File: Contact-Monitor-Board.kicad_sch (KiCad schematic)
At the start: 82 parts, among them J1 JST VH 02, J10 JST VH 02, J11 JST VH 02, J12 JST VH 02, J13 JST VH 02, J14 JST VH 02, J15 JST VH 02, J16 JST VH 02, J17 header 4, J2 JST VH 02, J3 JST VH 02, J4 JST VH 02, J5 JST VH 02, J6 JST VH 02, J7 JST VH 02, J8 JST VH 02, J9 JST VH 02, Q1 2N7002, Q10 2N7002, Q11 2N7002, Q12 2N7002, Q13 2N7002, Q14 2N7002, Q15 2N7002, Q16 2N7002, Q2 2N7002, Q3 2N7002, Q4 2N7002, Q5 2N7002, Q6 2N7002, Q7 2N7002, Q8 2N7002, Q9 2N7002, SW1 KH-SS12D01-G3-5.0, U1 74HC4017D, U2 TLC555CD, U3 TPS61222DCK

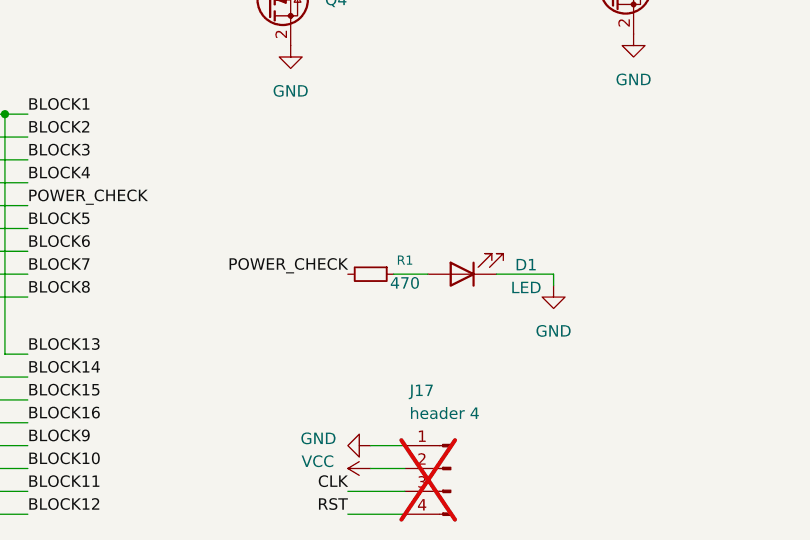
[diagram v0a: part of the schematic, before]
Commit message: 運転LED輝度調整 R1 470 -> 1k
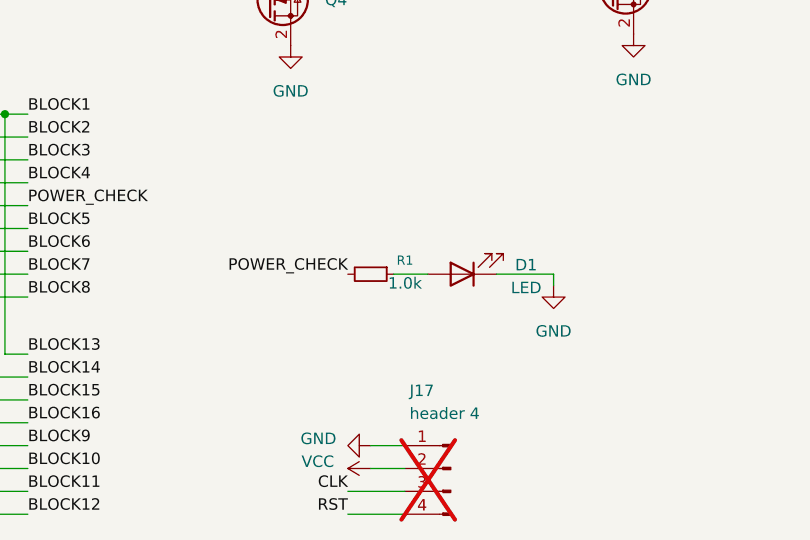
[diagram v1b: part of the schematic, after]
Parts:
- R1: value 470 -> 1.0k
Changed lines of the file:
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@@
 			)
 		)
-		(property "Value" "470"
+		(property "Value" "1.0k"
 			(at 156.21 153.416 90)
 			(effects
